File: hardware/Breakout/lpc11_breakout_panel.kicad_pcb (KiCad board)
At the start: 2 copper layers, 48.3 x 66.7 mm, 32 parts, among them J1 Conn_01x04_Male, J2 Conn_02x04_Odd_Even, J3 Conn_02x12_Odd_Even, J4 Conn_02x12_Odd_Even, J5 Conn_02x12_Odd_Even, J6 Conn_02x04_Odd_Even, U1 LPC1115JBD48-303, Y1 MCSJK-7U-12.00-10-10-80-B-10

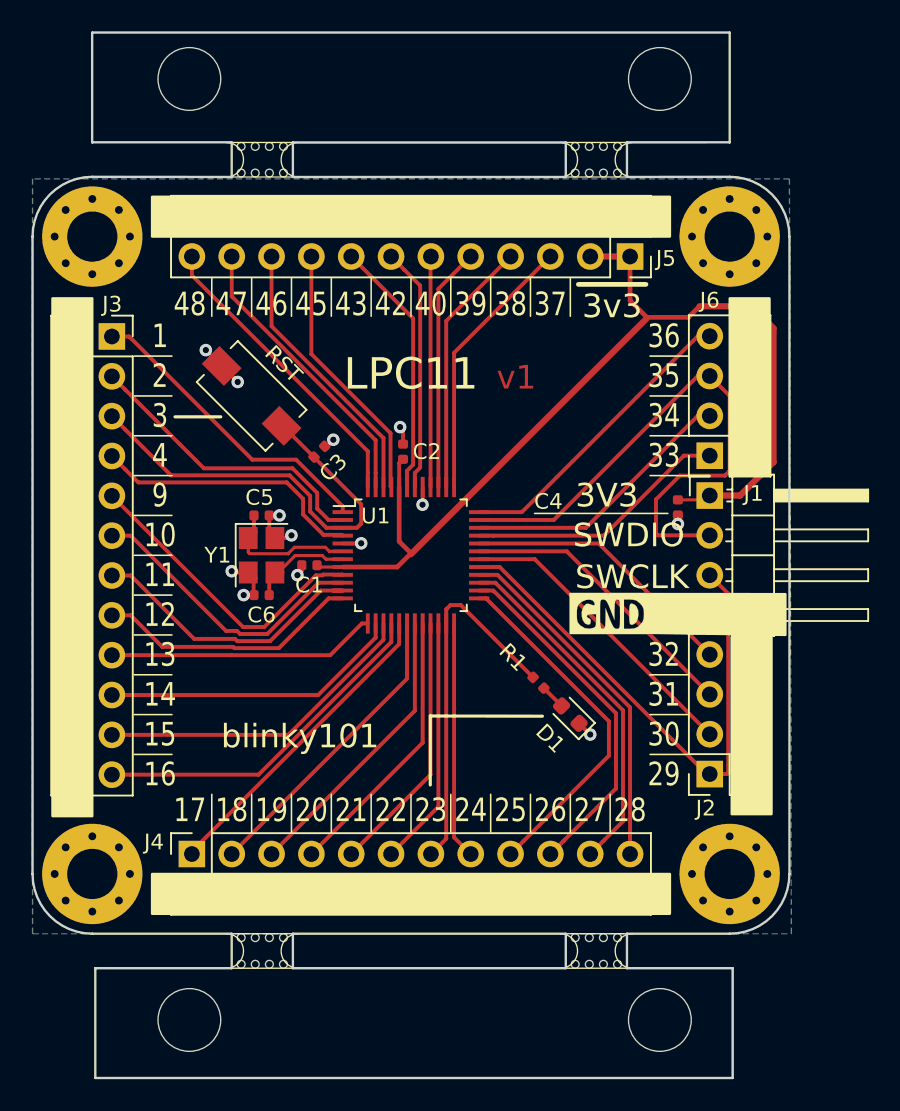
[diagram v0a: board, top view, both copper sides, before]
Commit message: Breakout PCB: Fix frame tooling hole-to-hole distance to multiple of 20mm
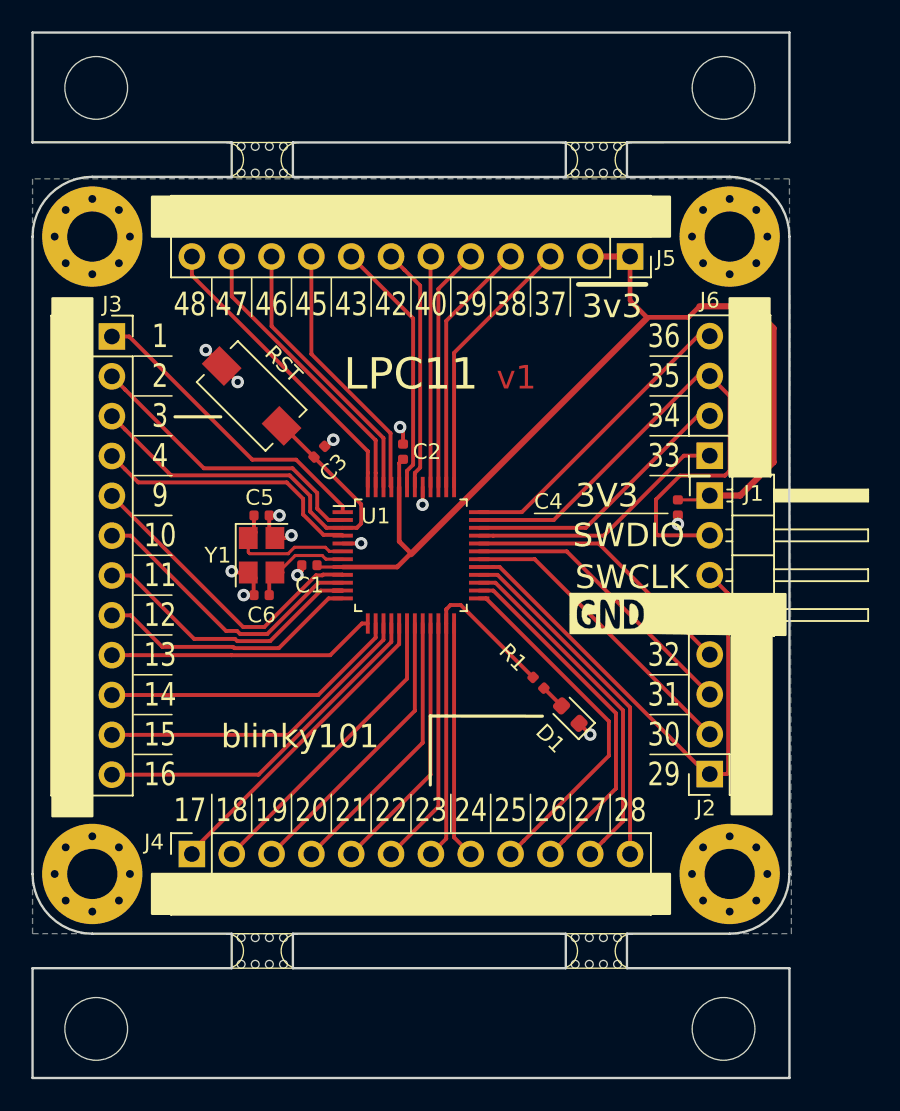
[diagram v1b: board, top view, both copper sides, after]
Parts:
- moved REF** 5.97 mm to (52.0, 90.0)
- moved REF** 5.97 mm to (52.0, 30.0)
- moved REF** 4.10 mm to (92.0, 30.0)
- moved REF** 4.10 mm to (92.0, 90.0)
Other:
- outline, holes or cut-outs redrawn
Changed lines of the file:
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@@
-(kicad_pcb (version 20171130) (host pcbnew "(5.0.2-5-10.14)")
+(kicad_pcb (version 20171130) (host pcbnew 5.0.2-bee76a0~70~ubuntu18.04.1)
   (general
     (thickness 1.6)
@@
     (visible_elements FFFFFF7F)
     (pcbplotparams
-      (layerselection 0x010fc_ffffffff)
+      (layerselection 0x010f0_ffffffff)
       (usegerberextensions false)
       (usegerberattributes false)
@@
   )
   (module Jitter_Footprints:Tooling_hole_4mm_4.04mm_paste locked (layer F.Cu)
-    (at 57.94 89.43)
+    (at 52 90)
     (fp_text reference REF** (at -4.8 -1.5) (layer F.SilkS) hide
       (effects (font (size 1 1) (thickness 0.15)))
@@
   )
   (module Jitter_Footprints:Tooling_hole_4mm_4.04mm_paste locked (layer F.Cu)
-    (at 87.94 89.43)
+    (at 92 90)
     (fp_text reference REF** (at -4.8 -1.5) (layer F.SilkS) hide
       (effects (font (size 1 1) (thickness 0.15)))
@@
   )
   (module Jitter_Footprints:Tooling_hole_4mm_4.04mm_paste locked (layer F.Cu)
-    (at 87.94 29.43)
+    (at 92 30)
     (fp_text reference REF** (at -4.8 -1.5) (layer F.SilkS) hide
       (effects (font (size 1 1) (thickness 0.15)))
@@
   )
   (module Jitter_Footprints:Tooling_hole_4mm_4.04mm_paste locked (layer F.Cu)
-    (at 57.94 29.43)
+    (at 52 30)
     (fp_text reference REF** (at -4.8 -1.5) (layer F.SilkS) hide
       (effects (font (size 1 1) (thickness 0.15)))
@@
     (pad "" np_thru_hole circle (at 1.95 7.2 90) (size 0.5 0.5) (drill 0.5) (layers *.Cu *.Mask))
   )
-  (gr_line (start 85.84 86.13) (end 92.58 86.13) (layer Edge.Cuts) (width 0.15))
+  (gr_line (start 85.84 86.13) (end 96.2 86.13) (layer Edge.Cuts) (width 0.15))
   (gr_line (start 81.94 83.93) (end 64.54 83.93) (layer Edge.Cuts) (width 0.15))
-  (gr_line (start 85.840015 33.472352) (end 92.39 33.47) (layer Edge.Cuts) (width 0.15))
+  (gr_line (start 85.840015 33.472352) (end 96.2 33.47) (layer Edge.Cuts) (width 0.15))
   (gr_line (start 85.84 35.68) (end 92.39 35.67) (layer Edge.Cuts) (width 0.15))
   (gr_line (start 64.54 35.68) (end 81.94 35.68) (layer Edge.Cuts) (width 0.15))
@@
   (gr_line (start 64.54 83.93) (end 64.54 86.13) (layer Edge.Cuts) (width 0.15))
   (gr_line (start 60.64 83.93) (end 60.64 86.13) (layer Edge.Cuts) (width 0.15))
-  (gr_line (start 51.74 26.48) (end 51.74 33.48) (layer Edge.Cuts) (width 0.15))
-  (gr_line (start 92.39 26.48) (end 92.39 33.48) (layer Edge.Cuts) (width 0.15))
-  (gr_line (start 92.58 86.13) (end 92.58 93.13) (layer Edge.Cuts) (width 0.15))
-  (gr_line (start 51.94 86.13) (end 51.94 93.13) (layer Edge.Cuts) (width 0.15))
-  (gr_line (start 51.75 26.47) (end 92.39 26.47) (layer Edge.Cuts) (width 0.15))
-  (gr_line (start 51.94 93.13) (end 92.58 93.13) (layer Edge.Cuts) (width 0.15))
-  (gr_line (start 51.94 86.13) (end 60.64 86.13) (layer Edge.Cuts) (width 0.15))
-  (gr_line (start 51.75 33.47) (end 60.64 33.47) (layer Edge.Cuts) (width 0.15))
+  (gr_line (start 47.94 26.48) (end 47.94 33.48) (layer Edge.Cuts) (width 0.15))
+  (gr_line (start 96.2 26.48) (end 96.2 33.48) (layer Edge.Cuts) (width 0.15))
+  (gr_line (start 96.2 86.13) (end 96.2 93.13) (layer Edge.Cuts) (width 0.15))
+  (gr_line (start 47.94 86.13) (end 47.94 93.13) (layer Edge.Cuts) (width 0.15))
+  (gr_line (start 47.94 26.47) (end 96.2 26.47) (layer Edge.Cuts) (width 0.15))
+  (gr_line (start 47.94 93.13) (end 96.2 93.13) (layer Edge.Cuts) (width 0.15))
+  (gr_line (start 47.94 86.13) (end 60.64 86.13) (layer Edge.Cuts) (width 0.15))
+  (gr_line (start 47.94 33.47) (end 60.64 33.47) (layer Edge.Cuts) (width 0.15))
   (gr_line (start 57.0205 50.9735) (end 59.9415 50.9735) (layer F.SilkS) (width 0.2))
   (gr_line (start 73.3 70.05) (end 80.45 70.06) (layer F.SilkS) (width 0.2))
